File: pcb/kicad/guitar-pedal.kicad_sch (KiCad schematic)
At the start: 5 parts, among them J1 USB_C_Receptacle_USB2.0

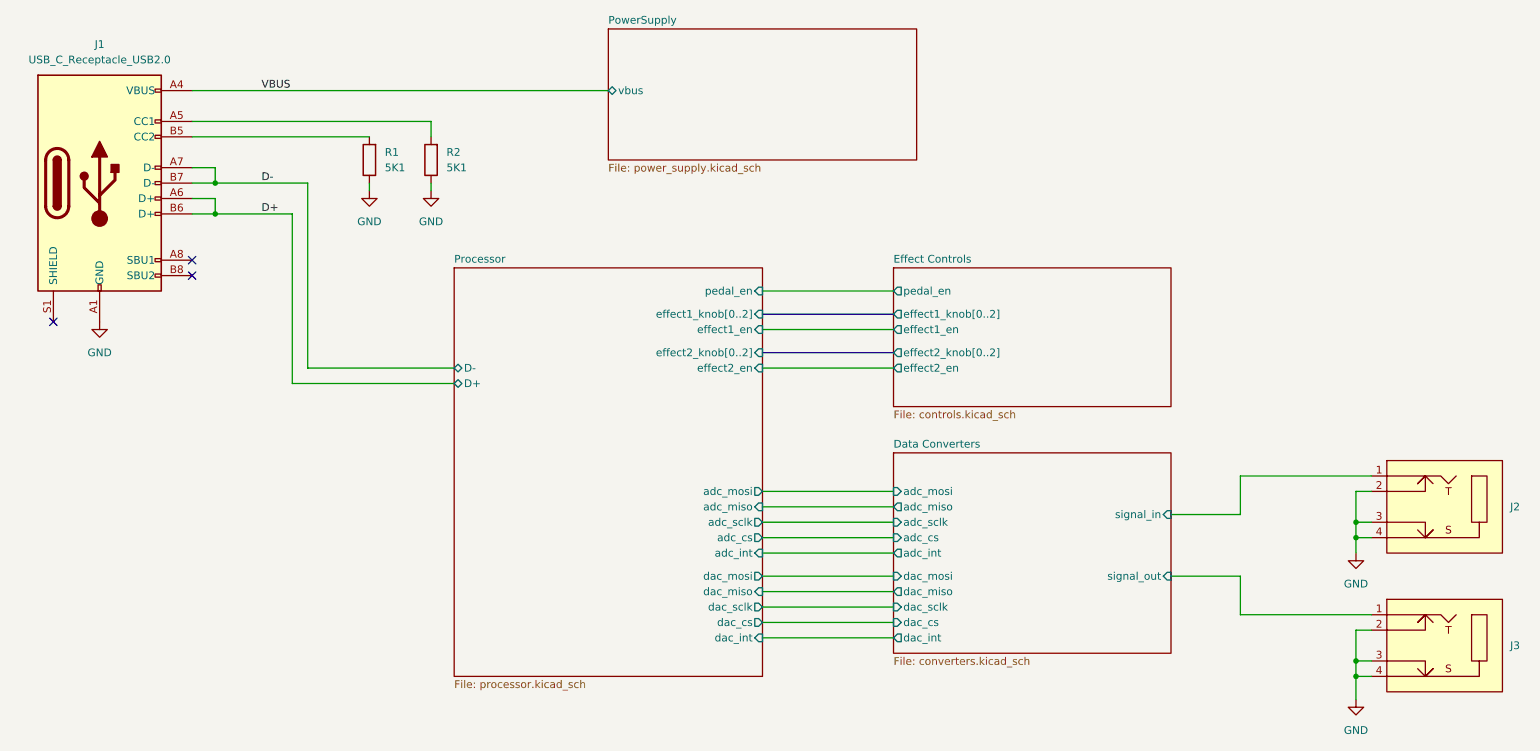
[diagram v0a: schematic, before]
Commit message: Move USB to own sheet.
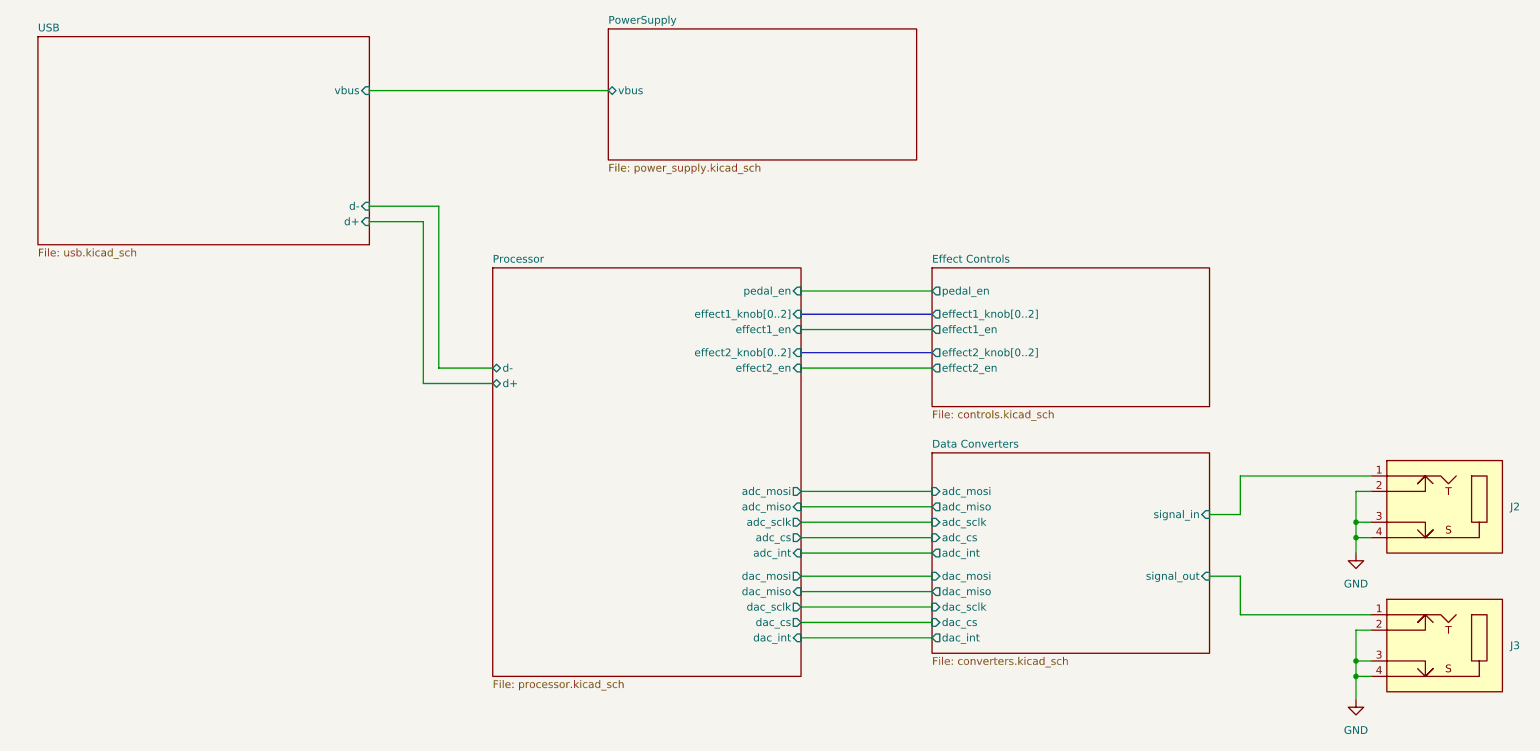
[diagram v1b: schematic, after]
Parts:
- removed J1: USB_C_Receptacle_USB2.0, symbol Connector:USB_C_Receptacle_USB2.0
- removed R1, R2: 5K1, Resistor_SMD:R_0805_2012Metric, symbol Device:R
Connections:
- no-connect marks 3 -> 0
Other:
- added sheet USB (usb.kicad_sch)
- sheet Processor ports: added d+, d-; removed D+, D-

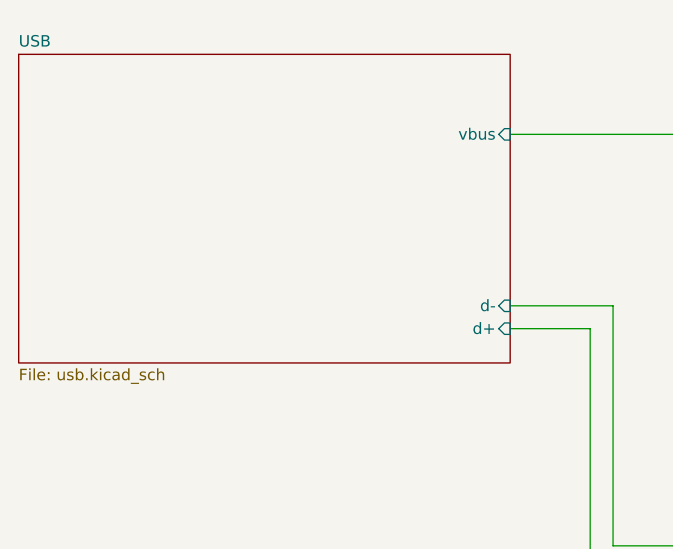
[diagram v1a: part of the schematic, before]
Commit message: Add SoC and pinout.
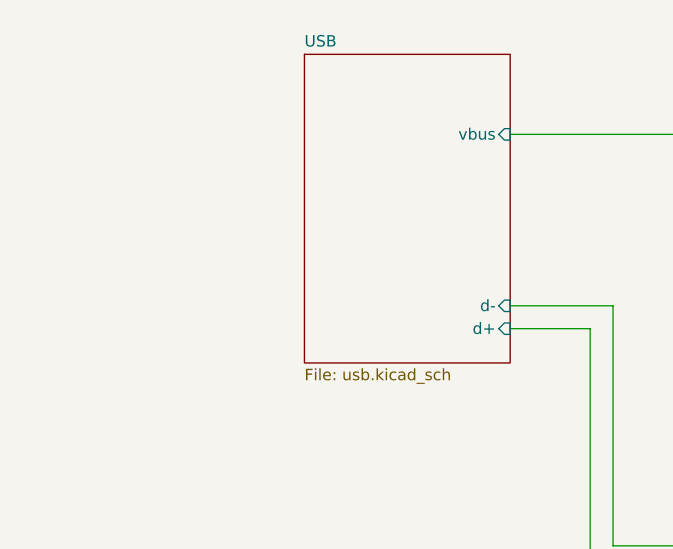
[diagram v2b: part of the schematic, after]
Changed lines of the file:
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@@
     )
   )
-  (sheet (at 26.67 46.99) (size 54.61 34.29) (fields_autoplaced)
+  (sheet (at 58.42 46.99) (size 22.86 34.29) (fields_autoplaced)
     (stroke (width 0.1524) (type solid))
     (fill (color 0 0 0 0.0000))
-    (property "Sheetname" "USB" (at 26.67 46.2784 0)
+    (property "Sheetname" "USB" (at 58.42 46.2784 0)
       (effects (font (size 1.27 1.27)) (justify left bottom))
     )
-    (property "Sheetfile" "usb.kicad_sch" (at 26.67 81.8646 0)
+    (property "Sheetfile" "usb.kicad_sch" (at 58.42 81.8646 0)
       (effects (font (size 1.27 1.27)) (justify left top))
     )

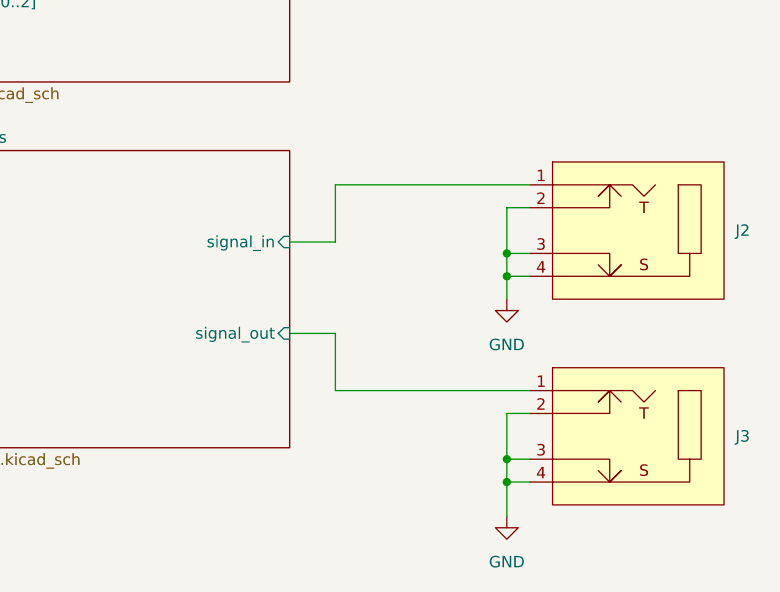
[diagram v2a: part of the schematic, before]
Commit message: Added ADC digital part.
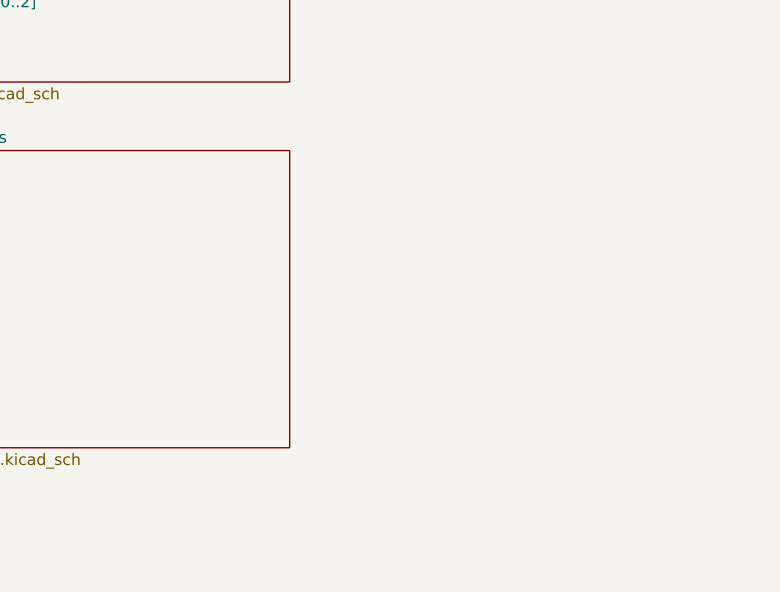
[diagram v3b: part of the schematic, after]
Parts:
- removed J2, J3: ~, symbol pedal-components:NMJ4HCD2
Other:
- sheet Data Converters ports: added none; removed signal_in, signal_out
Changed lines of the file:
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@@
 (kicad_sch (version 20230121) (generator eeschema)
   (paper "A4")
-  (junction (at 243.84 129.54) (diameter 0) (color 0 0 0 0)
-  )
-  (junction (at 243.84 149.86) (diameter 0) (color 0 0 0 0)
-  )
-  (junction (at 243.84 127) (diameter 0) (color 0 0 0 0)
-  )
-  (junction (at 243.84 152.4) (diameter 0) (color 0 0 0 0)
-  )
-  (wire (pts (xy 224.79 119.38) (xy 224.79 125.73))
-    (stroke (width 0) (type default))
-  )
   (wire (pts (xy 81.28 77.47) (xy 90.17 77.47))
     (stroke (width 0) (type default))
   )
-  (wire (pts (xy 243.84 149.86) (xy 246.38 149.86))
-    (stroke (width 0) (type default))
-  )
   (bus (pts (xy 152.4 92.71) (xy 173.99 92.71))
-    (stroke (width 0) (type default))
-  )
-  (wire (pts (xy 246.38 121.92) (xy 243.84 121.92))
-    (stroke (width 0) (type default))
-  )
-  (wire (pts (xy 219.71 125.73) (xy 224.79 125.73))
     (stroke (width 0) (type default))
   )
@@
     (stroke (width 0) (type default))
   )
-  (wire (pts (xy 246.38 142.24) (xy 224.79 142.24))
-    (stroke (width 0) (type default))
-  )
   (wire (pts (xy 92.71 74.93) (xy 92.71 101.6))
-    (stroke (width 0) (type default))
-  )
-  (wire (pts (xy 243.84 129.54) (xy 243.84 132.08))
     (stroke (width 0) (type default))
   )
@@
     (stroke (width 0) (type default))
   )
-  (wire (pts (xy 243.84 127) (xy 243.84 129.54))
-    (stroke (width 0) (type default))
-  )
   (wire (pts (xy 152.4 124.46) (xy 173.99 124.46))
-    (stroke (width 0) (type default))
-  )
-  (wire (pts (xy 243.84 144.78) (xy 243.84 149.86))
     (stroke (width 0) (type default))
   )
@@
   )
   (wire (pts (xy 92.71 101.6) (xy 101.6 101.6))
-    (stroke (width 0) (type default))
-  )
-  (wire (pts (xy 246.38 129.54) (xy 243.84 129.54))
-    (stroke (width 0) (type default))
-  )
-  (wire (pts (xy 243.84 121.92) (xy 243.84 127))
-    (stroke (width 0) (type default))
-  )
-  (wire (pts (xy 243.84 149.86) (xy 243.84 152.4))
-    (stroke (width 0) (type default))
-  )
-  (wire (pts (xy 243.84 152.4) (xy 246.38 152.4))
     (stroke (width 0) (type default))
   )
@@
   )
   (wire (pts (xy 152.4 132.08) (xy 173.99 132.08))
-    (stroke (width 0) (type default))
-  )
-  (wire (pts (xy 246.38 144.78) (xy 243.84 144.78))
     (stroke (width 0) (type default))
   )
@@
     (stroke (width 0) (type default))
   )
-  (wire (pts (xy 243.84 152.4) (xy 243.84 156.21))
-    (stroke (width 0) (type default))
-  )
-  (wire (pts (xy 219.71 135.89) (xy 224.79 135.89))
-    (stroke (width 0) (type default))
-  )
   (wire (pts (xy 152.4 129.54) (xy 173.99 129.54))
     (stroke (width 0) (type default))
   )
   (wire (pts (xy 152.4 138.43) (xy 173.99 138.43))
-    (stroke (width 0) (type default))
-  )
-  (wire (pts (xy 246.38 119.38) (xy 224.79 119.38))
     (stroke (width 0) (type default))
   )
@@
     (stroke (width 0) (type default))
   )
-  (wire (pts (xy 224.79 142.24) (xy 224.79 135.89))
-    (stroke (width 0) (type default))
-  )
   (wire (pts (xy 81.28 74.93) (xy 92.71 74.93))
     (stroke (width 0) (type default))
-  )
-  (wire (pts (xy 246.38 127) (xy 243.84 127))
-    (stroke (width 0) (type default))
-  )
-  (symbol (lib_id "pedal-components:NMJ4HCD2") (at 248.92 147.32 0) (unit 1)
-    (in_bom yes) (on_board yes) (dnp no) (fields_autoplaced)
-    (property "Reference" "J3" (at 269.24 147.32 0)
-      (effects (font (size 1.27 1.27)) (justify left))
-    )
-    (property "Value" "~" (at 248.92 147.32 0)
-      (effects (font (size 1.27 1.27)))
-    )
-    (property "Footprint" "" (at 248.92 147.32 0)
-      (effects (font (size 1.27 1.27)) hide)
-    )
-    (property "Datasheet" "" (at 248.92 147.32 0)
-      (effects (font (size 1.27 1.27)) hide)
-    )
-    (pin "1")
-    (pin "2")
-    (pin "3")
-    (pin "4")
-    (instances
-      (project "guitar-pedal"
-        (path "/aeca30b5-691d-475f-a243-a02c48b6690c"
-          (reference "J3") (unit 1)
-        )
-      )
-    )
-  )
-  (symbol (lib_id "pedal-components:NMJ4HCD2") (at 248.92 124.46 0) (unit 1)
-    (in_bom yes) (on_board yes) (dnp no) (fields_autoplaced)
-    (property "Reference" "J2" (at 269.24 124.46 0)
-      (effects (font (size 1.27 1.27)) (justify left))
-    )
-    (property "Value" "~" (at 248.92 124.46 0)
-      (effects (font (size 1.27 1.27)))
-    )
-    (property "Footprint" "" (at 248.92 124.46 0)
-      (effects (font (size 1.27 1.27)) hide)
-    )
-    (property "Datasheet" "" (at 248.92 124.46 0)
-      (effects (font (size 1.27 1.27)) hide)
-    )
-    (pin "1")
-    (pin "2")
-    (pin "3")
-    (pin "4")
-    (instances
-      (project "guitar-pedal"
-        (path "/aeca30b5-691d-475f-a243-a02c48b6690c"
-          (reference "J2") (unit 1)
-        )
-      )
-    )
-  )
-  (symbol (lib_id "power:GND") (at 243.84 156.21 0) (unit 1)
-    (in_bom yes) (on_board yes) (dnp no) (fields_autoplaced)
-    (property "Reference" "#PWR05" (at 243.84 162.56 0)
-      (effects (font (size 1.27 1.27)) hide)
-    )
-    (property "Value" "GND" (at 243.84 161.29 0)
-      (effects (font (size 1.27 1.27)))
-    )
-    (property "Footprint" "" (at 243.84 156.21 0)
-      (effects (font (size 1.27 1.27)) hide)
-    )
-    (property "Datasheet" "" (at 243.84 156.21 0)
-      (effects (font (size 1.27 1.27)) hide)
-    )
-    (pin "1")
-    (instances
-      (project "guitar-pedal"
-        (path "/aeca30b5-691d-475f-a243-a02c48b6690c"
-          (reference "#PWR05") (unit 1)
-        )
-      )
-    )
-  )
-  (symbol (lib_id "power:GND") (at 243.84 132.08 0) (unit 1)
-    (in_bom yes) (on_board yes) (dnp no) (fields_autoplaced)
-    (property "Reference" "#PWR04" (at 243.84 138.43 0)
-      (effects (font (size 1.27 1.27)) hide)
-    )
-    (property "Value" "GND" (at 243.84 137.16 0)
-      (effects (font (size 1.27 1.27)))
-    )
-    (property "Footprint" "" (at 243.84 132.08 0)
-      (effects (font (size 1.27 1.27)) hide)
-    )
-    (property "Datasheet" "" (at 243.84 132.08 0)
-      (effects (font (size 1.27 1.27)) hide)
-    )
-    (pin "1")
-    (instances
-      (project "guitar-pedal"
-        (path "/aeca30b5-691d-475f-a243-a02c48b6690c"
-          (reference "#PWR04") (unit 1)
-        )
-      )
-    )
   )
   (sheet (at 173.99 115.57) (size 45.72 33.02) (fields_autoplaced)
@@
       (effects (font (size 1.27 1.27)) (justify left))
     )
-    (pin "signal_in" input (at 219.71 125.73 0)
-      (effects (font (size 1.27 1.27)) (justify right))
-    )
-    (pin "signal_out" input (at 219.71 135.89 0)
-      (effects (font (size 1.27 1.27)) (justify right))
-    )
     (instances

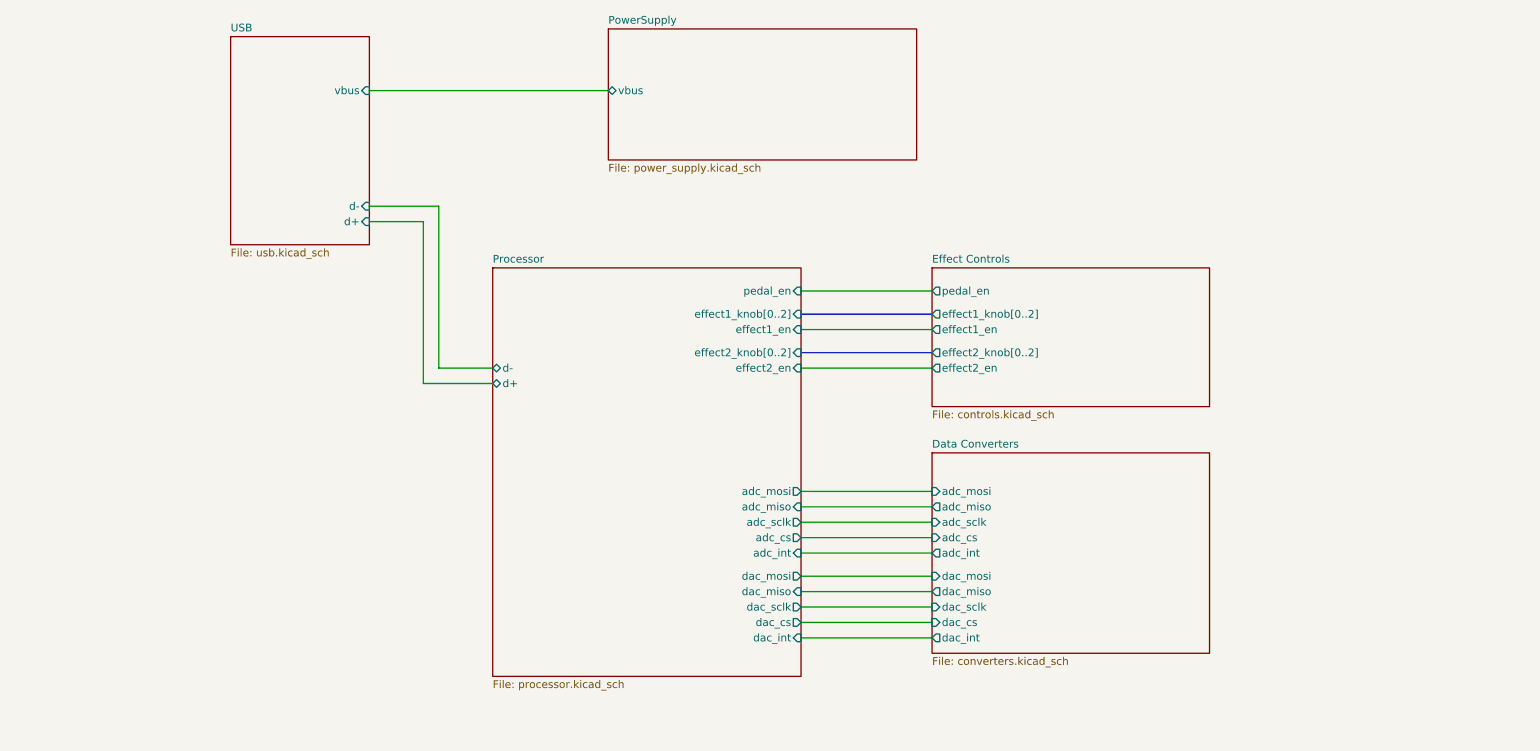
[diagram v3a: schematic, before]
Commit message: Added converters, controls and updated annotations.
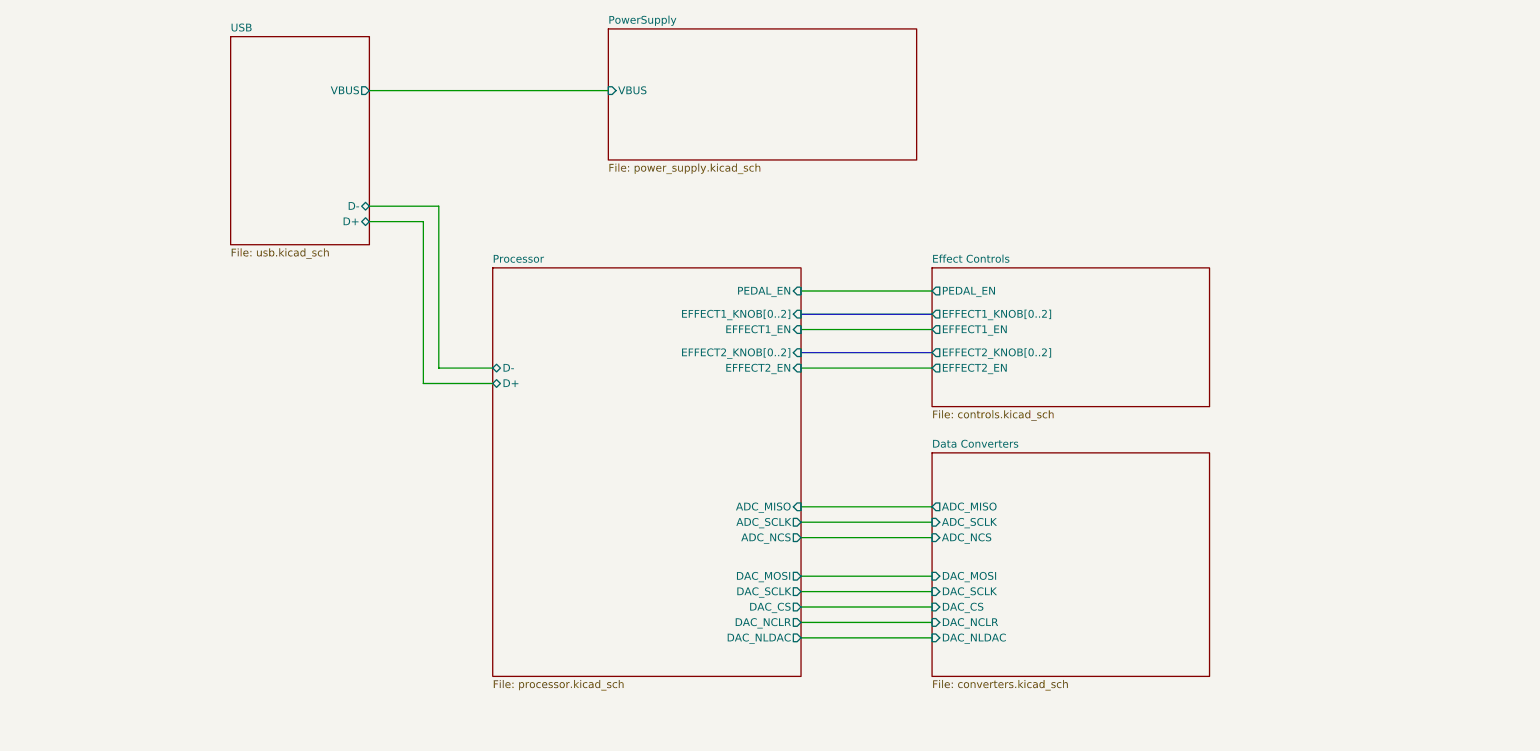
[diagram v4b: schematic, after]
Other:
- sheet Data Converters ports: added ADC_MISO, ADC_NCS, ADC_SCLK, DAC_CS, DAC_MOSI, DAC_NCLR, DAC_NLDAC, DAC_SCLK; removed adc_cs, adc_int, adc_miso, adc_mosi, adc_sclk, dac_cs, dac_int, dac_miso, dac_mosi, dac_sclk
- sheet Effect Controls ports: added EFFECT1_EN, EFFECT1_KNOB[0..2], EFFECT2_EN, EFFECT2_KNOB[0..2], PEDAL_EN; removed effect1_en, effect1_knob[0..2], effect2_en, effect2_knob[0..2], pedal_en
- sheet PowerSupply ports: added VBUS; removed vbus
- sheet Processor ports: added ADC_MISO, ADC_NCS, ADC_SCLK, D+, D-, DAC_CS, DAC_MOSI, DAC_NCLR, DAC_NLDAC, DAC_SCLK, EFFECT1_EN, EFFECT1_KNOB[0..2], EFFECT2_EN, EFFECT2_KNOB[0..2], PEDAL_EN; removed adc_cs, adc_int, adc_miso, adc_mosi, adc_sclk, d+, d-, dac_cs, dac_int, dac_miso, dac_mosi, dac_sclk, effect1_en, effect1_knob[0..2], effect2_en, effect2_knob[0..2], pedal_en
- sheet USB ports: added D+, D-, VBUS; removed d+, d-, vbus
